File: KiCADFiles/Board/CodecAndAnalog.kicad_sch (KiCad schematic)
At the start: 37 parts, among them J1 XLR, J2 MONO JACK, J4 MONO JACK, J5 MONO JACK, J6 MONO JACK, J7 MONO JACK, K2 Fujitsu_FTR-LYCA005x, U5 CS4272, U9 OPA1655D, X1 24.576 MHz 20 pF

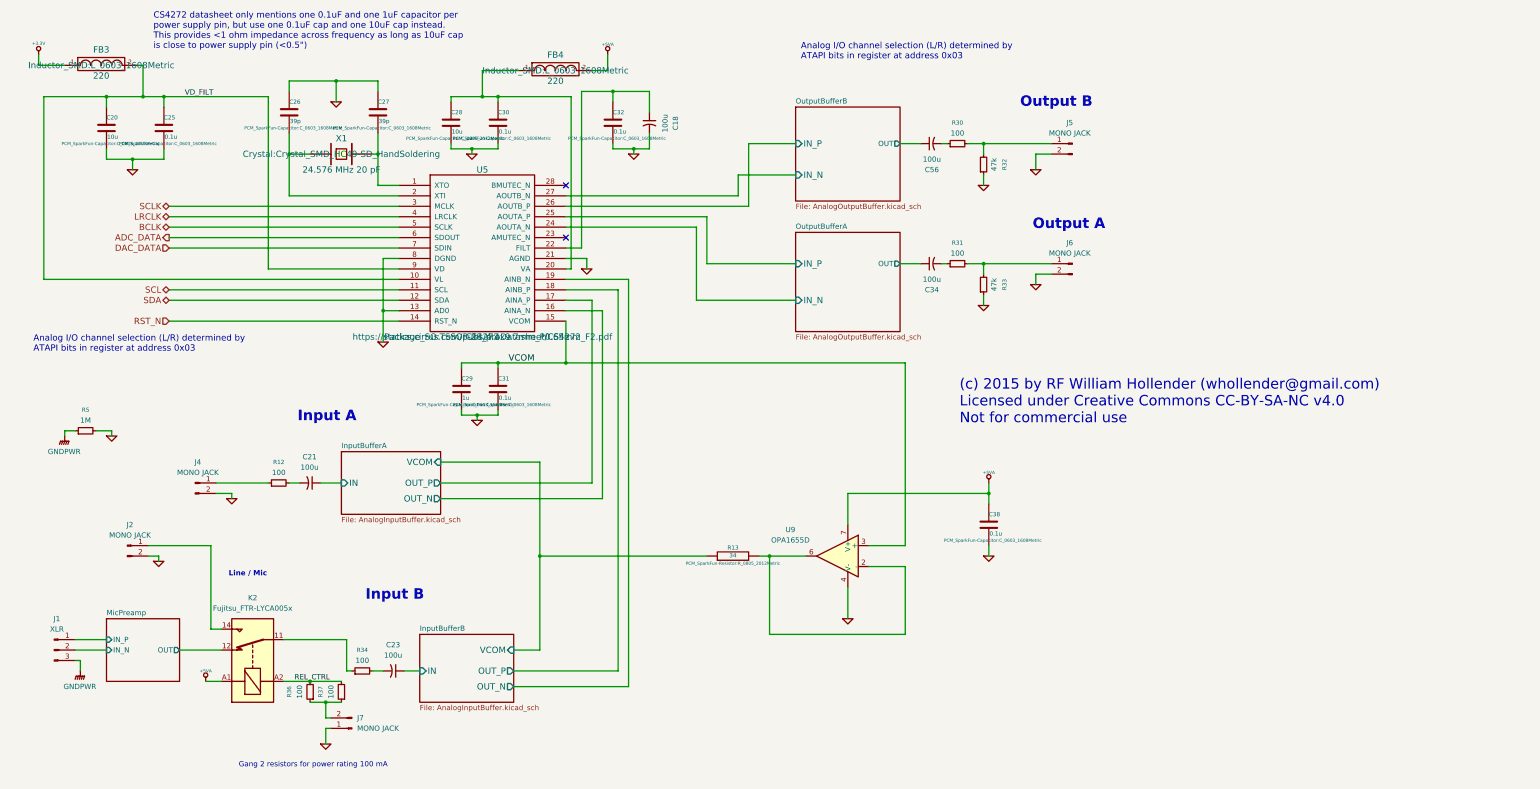
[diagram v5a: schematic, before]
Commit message: finished layout, passed DRC
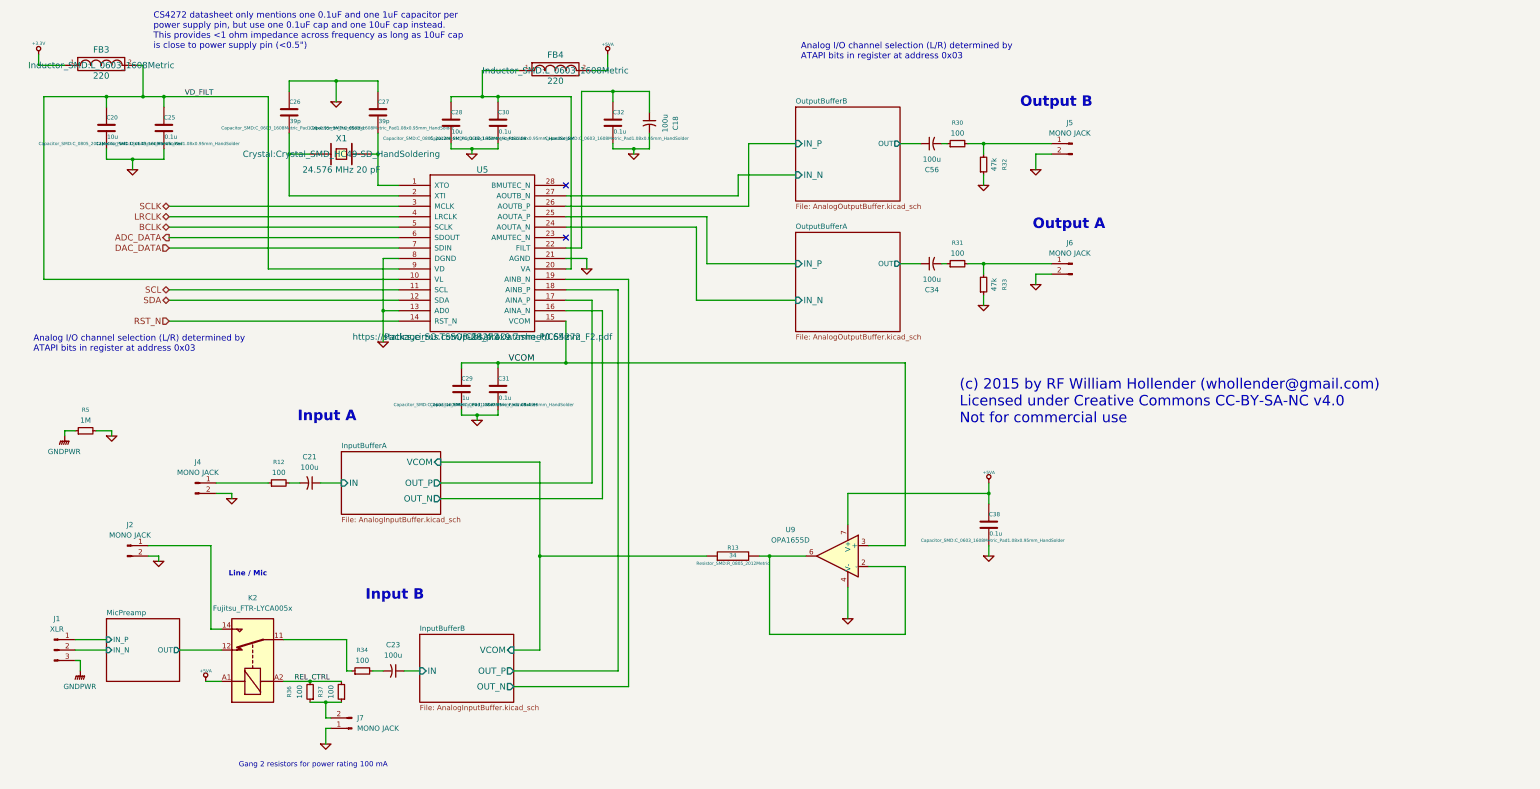
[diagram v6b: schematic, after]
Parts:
- C20, C28: footprint PCM_SparkFun-Capacitor:C_0805_2012Metric -> Capacitor_SMD:C_0805_2012Metric_Pad1.18x1.45mm_HandSolder
- C25, C26, C27, C29, C30, C31, C32, C38: footprint PCM_SparkFun-Capacitor:C_0603_1608Metric -> Capacitor_SMD:C_0603_1608Metric_Pad1.08x0.95mm_HandSolder
- R12, R13, R30, R31, R32, R33, R34, R36, R37, R5: footprint PCM_SparkFun-Resistor:R_0805_2012Metric -> Resistor_SMD:R_0805_2012Metric
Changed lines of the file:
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@@
 			)
 		)
-		(property "Footprint" "PCM_SparkFun-Capacitor:C_0603_1608Metric"
+		(property "Footprint" "Capacitor_SMD:C_0603_1608Metric_Pad1.08x0.95mm_HandSolder"
 			(at 79.7052 36.83 0)
 			(effects
@@
 			)
 		)
-		(property "Footprint" "PCM_SparkFun-Capacitor:C_0603_1608Metric"
+		(property "Footprint" "Capacitor_SMD:C_0603_1608Metric_Pad1.08x0.95mm_HandSolder"
 			(at 158.4452 39.37 0)
 			(effects
@@
 			)
 		)
-		(property "Footprint" "PCM_SparkFun-Capacitor:C_0603_1608Metric"
+		(property "Footprint" "Capacitor_SMD:C_0603_1608Metric_Pad1.08x0.95mm_HandSolder"
 			(at 121.6152 104.14 0)
 			(effects
@@
 			)
 		)
-		(property "Footprint" "PCM_SparkFun-Resistor:R_0805_2012Metric"
+		(property "Footprint" "Resistor_SMD:R_0805_2012Metric"
 			(at 186.69 142.748 90)
 			(effects
@@
 			)
 		)
-		(property "Footprint" "PCM_SparkFun-Capacitor:C_0603_1608Metric"
+		(property "Footprint" "Capacitor_SMD:C_0603_1608Metric_Pad1.08x0.95mm_HandSolder"
 			(at 130.5052 39.37 0)
 			(effects
@@
 			)
 		)
-		(property "Footprint" "PCM_SparkFun-Capacitor:C_0603_1608Metric"
+		(property "Footprint" "Capacitor_SMD:C_0603_1608Metric_Pad1.08x0.95mm_HandSolder"
 			(at 49.2252 40.64 0)
 			(effects
@@
 			)
 		)
-		(property "Footprint" "PCM_SparkFun-Capacitor:C_0603_1608Metric"
+		(property "Footprint" "Capacitor_SMD:C_0603_1608Metric_Pad1.08x0.95mm_HandSolder"
 			(at 130.5052 104.14 0)
 			(effects
@@
 			)
 		)
-		(property "Footprint" "PCM_SparkFun-Capacitor:C_0603_1608Metric"
+		(property "Footprint" "Capacitor_SMD:C_0603_1608Metric_Pad1.08x0.95mm_HandSolder"
 			(at 249.8852 137.16 0)
 			(effects
@@
 			)
 		)
-		(property "Footprint" "PCM_SparkFun-Capacitor:C_0805_2012Metric"
+		(property "Footprint" "Capacitor_SMD:C_0805_2012Metric_Pad1.18x1.45mm_HandSolder"
 			(at 35.2552 40.64 0)
 			(effects
@@
 			)
 		)
-		(property "Footprint" "PCM_SparkFun-Capacitor:C_0805_2012Metric"
+		(property "Footprint" "Capacitor_SMD:C_0805_2012Metric_Pad1.18x1.45mm_HandSolder"
 			(at 119.0752 39.37 0)
 			(effects
@@
 			)
 		)
-		(property "Footprint" "PCM_SparkFun-Capacitor:C_0603_1608Metric"
+		(property "Footprint" "Capacitor_SMD:C_0603_1608Metric_Pad1.08x0.95mm_HandSolder"
 			(at 101.2952 36.83 0)
 			(effects
@@
 			)
 		)
-		(property "Footprint" "PCM_SparkFun-Resistor:R_0805_2012Metric"
+		(property "Footprint" "Resistor_SMD:R_0805_2012Metric"
 			(at 247.65 45.72 0)
 			(effects
@@
 			)
 		)
-		(property "Footprint" "PCM_SparkFun-Resistor:R_0805_2012Metric"
+		(property "Footprint" "Resistor_SMD:R_0805_2012Metric"
 			(at 247.65 74.93 0)
 			(effects
@@
 			)
 		)
-		(property "Footprint" "PCM_SparkFun-Resistor:R_0805_2012Metric"
+		(property "Footprint" "Resistor_SMD:R_0805_2012Metric"
 			(at 91.44 173.99 0)
 			(effects
@@
 			)
 		)
-		(property "Footprint" "PCM_SparkFun-Resistor:R_0805_2012Metric"
+		(property "Footprint" "Resistor_SMD:R_0805_2012Metric"
 			(at 241.3 40.64 0)
 			(effects
@@
 			)
 		)
-		(property "Footprint" "PCM_SparkFun-Resistor:R_0805_2012Metric"
+		(property "Footprint" "Resistor_SMD:R_0805_2012Metric"
 			(at 29.21 110.49 0)
 			(effects
@@
 			)
 		)
-		(property "Footprint" "PCM_SparkFun-Resistor:R_0805_2012Metric"
+		(property "Footprint" "Resistor_SMD:R_0805_2012Metric"
 			(at 96.52 168.91 0)
 			(effects
@@
 			)
 		)
-		(property "Footprint" "PCM_SparkFun-Resistor:R_0805_2012Metric"
+		(property "Footprint" "Resistor_SMD:R_0805_2012Metric"
 			(at 241.3 69.85 0)
 			(effects
@@
 			)
 		)
-		(property "Footprint" "PCM_SparkFun-Resistor:R_0805_2012Metric"
+		(property "Footprint" "Resistor_SMD:R_0805_2012Metric"
 			(at 76.2 123.19 0)
 			(effects
@@
 			)
 		)
-		(property "Footprint" "PCM_SparkFun-Resistor:R_0805_2012Metric"
+		(property "Footprint" "Resistor_SMD:R_0805_2012Metric"
 			(at 83.82 173.99 0)
 			(effects
